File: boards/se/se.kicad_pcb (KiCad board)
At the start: 2 copper layers, 97.2 x 56.5 mm, 35 parts, among them J1 SE_PDS, J2 Conn_02x05_Odd_Even, U1 ENC624J600-PT, U3 GAL16V8, U5 LD1117S33TR_SOT223, Y1 25MHz

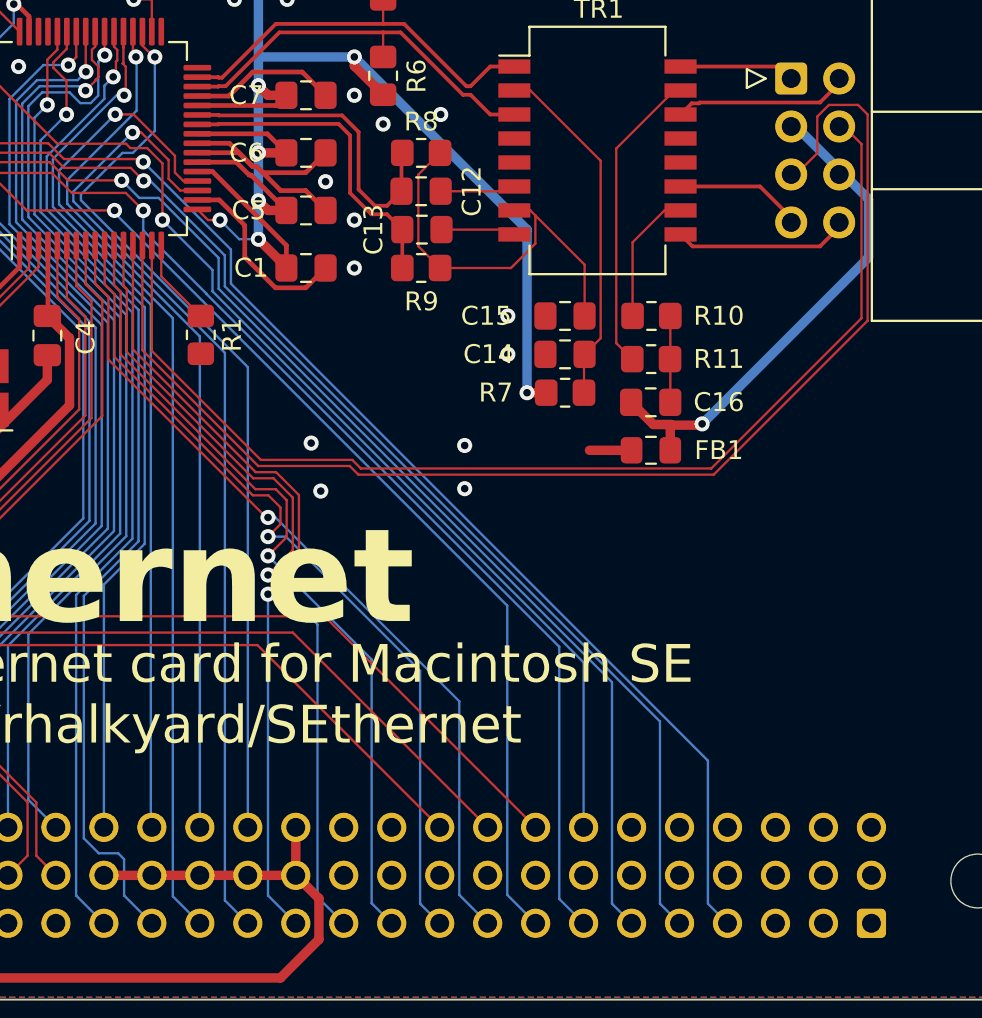
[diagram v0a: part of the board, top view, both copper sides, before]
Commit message: SE: fiddle some track positions for better fills
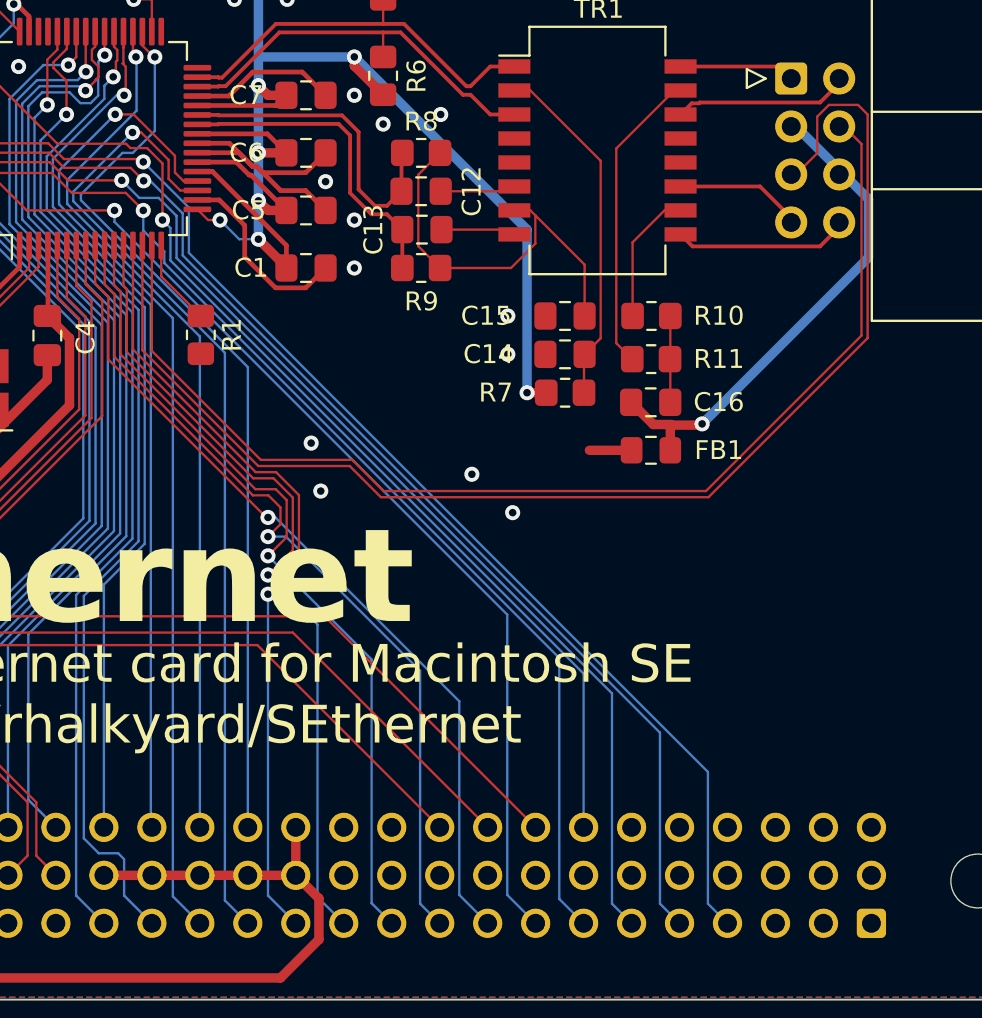
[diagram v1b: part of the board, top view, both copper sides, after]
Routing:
- net /LEDB: track 67.6 -> 69.2 mm
- net /LEDA: track 59.6 -> 61.1 mm

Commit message: Rev1 hardware
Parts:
- added C10: 1uF, Capacitor_SMD:C_0805_2012Metric_Pad1.18x1.45mm_HandSolder, B.Cu at (88.9, 77.7)
- added C11: 1uF, Capacitor_SMD:C_0805_2012Metric_Pad1.18x1.45mm_HandSolder, B.Cu at (77.7, 86.4)
- added C12: 1uF, Capacitor_SMD:C_0805_2012Metric_Pad1.18x1.45mm_HandSolder, B.Cu at (100.1, 89.4)
- added C19: 1uF, Capacitor_SMD:C_0805_2012Metric_Pad1.18x1.45mm_HandSolder, B.Cu at (87.6, 100.1)
- added J3: Conn_01x07, Connector_PinHeader_2.54mm:PinHeader_1x07_P2.54mm_Vertical, F.Cu at (88.9, 113.0)
- added U2: ATF1502AS-xAx44, Package_QFP:TQFP-44_10x10mm_P0.8mm, B.Cu at (88.9, 88.9)
- C1: renamed from C16; footprint Capacitor_SMD:C_0805_2012Metric_Pad1.18x1.45mm_HandSolder -> Capacitor_SMD:C_1206_3216Metric_Pad1.33x1.80mm_HandSolder; moved to B.Cu
- C13: renamed from C4; moved to B.Cu
- C14: renamed from C2; moved to B.Cu
- C15: renamed from C10; moved to B.Cu
- C16: renamed from C8; moved to B.Cu
- C17: renamed from C3; moved to B.Cu
- C18: renamed from C9; moved to B.Cu
- C2: renamed from C15; moved to B.Cu
- C20: renamed from C11; moved to B.Cu
- C21: renamed from C18; moved to B.Cu
- C22: renamed from C17; moved to B.Cu
- C3: renamed from C14; moved to B.Cu
- C4: renamed from C13; moved to B.Cu
- C5: renamed from C12; moved to B.Cu
- C6: renamed from C1; moved to B.Cu
- C7: renamed from C5; moved to B.Cu
- C8: renamed from C6; moved to B.Cu
- C9: renamed from C7; moved to B.Cu
- FB1, J2, R6, TR1, U1, Y1: moved to B.Cu
- J1: value SE_PDS -> Macintosh SE PDS Interface; footprint Connector_DIN:DIN41612_C_3x32_Female_Vertical_THT -> PDS-Ethernet:DIN41612_C_3x32_Female_Vertical_THT_Reversed
- R1: renamed from R10; moved to B.Cu
- R2: renamed from R11; moved to B.Cu
- R3: renamed from R7; moved to B.Cu
- R4: renamed from R9; moved to B.Cu
- R5: renamed from R8; moved to B.Cu
- R7: renamed from R4; moved to B.Cu
- R8: renamed from R1; moved to B.Cu
- R9: renamed from R5; moved to B.Cu
- U3: value GAL16V8 -> 74LVC2G17; footprint Package_LCC:PLCC-20_THT-Socket -> Package_TO_SOT_SMD:SOT-363_SC-70-6; moved to B.Cu
- U4: renamed from U5; moved to B.Cu
- moved C21 88.3 mm to (97.6, 113.0)
- moved C22 86.1 mm to (106.4, 113.0)
- moved U4 82.6 mm to (101.9, 106.8), turned to 180 degrees
- moved U3 77.0 mm to (76.8, 93.4), turned to 180 degrees
- moved C16 71.3 mm to (76.8, 96.5)
- moved C14 70.6 mm to (69.6, 91.7)
- moved C18 67.6 mm to (56.6, 100.8), turned to -90 degrees
- moved C17 65.2 mm to (52.9, 100.8), turned to 90 degrees
- moved R9 64.2 mm to (69.6, 85.1)
- moved U1 60.1 mm to (57.7, 88.9), turned to 0 degrees
- moved C15 56.8 mm to (47.0, 94.0), turned to 0 degrees
- moved Y1 56.8 mm to (47.0, 97.8), turned to 180 degrees
- moved C20 56.8 mm to (47.0, 101.6), turned to 180 degrees
- moved C13 54.9 mm to (47.0, 91.4), turned to 0 degrees
- moved C9 54.1 mm to (59.9, 77.5), turned to 90 degrees
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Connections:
- J1 pad b28: unconnected-(J1-~{EXT_DTK}-Padb28) -> ~{EXT_DTK}
- J1 pad c12: unconnected-(J1-~{RESET}-Padc12) -> ~{RESET}
- J1 pad c6: unconnected-(J1-~{DTACK}-Padc6) -> ~{DTACK}
- R9 pad 1: +3.3V -> GND
- U1 pad 33: unconnected-(U1-CLKOUT-Pad33) -> /ETH_CLK
- U1 pad 48: /B1SEL -> /B1SEL'
- U1 pad 49: Net-(U1-~{CS}/CS) -> /ETH_CS
- U1 pad 50: /B0SEL -> /B0SEL'
- U3 pad 1: A23 -> /B1SEL
- U3 pad 2: A22 -> GND
- U3 pad 3: A21 -> /B0SEL
- U3 pad 4: A20 -> /B0SEL'
- U3 pad 5: A19 -> +5V
- U3 pad 6: A18 -> /B1SEL'
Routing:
- net GND: track 76.8 -> 162.7 mm, vias 37 -> 160
- net ~{EXT_DTK}: track 0.00 -> 52.3 mm, vias 0 -> 1
- net ~{UDS}: track 73.5 -> 24.7 mm, vias 1 -> 0
- net ~{LDS}: track 72.6 -> 25.8 mm, vias 1 -> 0
- net ~{AS}: track 63.8 -> 24.1 mm, vias 1 -> 0
- net /CPLD_VPP: track 0.00 -> 36.6 mm, vias 0 -> 1
- net D12: track 43.7 -> 79.7 mm
- net +5V: track 128.5 -> 164.3 mm, vias 2 -> 0
- net D13: track 46.0 -> 80.6 mm
- net Net-(U1-~{CS}/CS): track 34.5 -> 0.00 mm, vias 1 -> 0
- net /TCK: track 0.00 -> 33.8 mm, vias 0 -> 1
- net D14: track 47.7 -> 81.2 mm
- net D15: track 48.8 -> 81.9 mm
- net /TPOUT-: track 21.1 -> 52.7 mm
- net /TPOUT+: track 21.1 -> 52.6 mm
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- added copper zone on In1.Cu, net GND
- added copper zone on In2.Cu, net GND
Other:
- board size 97.2 x 56.5 mm -> 90 x 99 mm
- copper layers 2 -> 4
- board text added: "+5V"
- board text added: "10/100 Ethernet for Macintosh SE github.com/rhalkyard/SEthernet Revision 1"
- board text added: "3"
- board text added: "Build info:"
- board text added: "CPLD JTAG"
- board text added: "GND"
- board text added: "TCK"
- board text added: "TDI"
- board text added: "TDO"
- board text added: "TMS"
- board text added: "V_{PP}"
- board text removed: "10/100 Ethernet card for Macintosh SE github.com/rhalkyard/SEthernet"
- board text removed: "Revision 0"

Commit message: SPISEL pulldown resistor should be 100K, not 10K
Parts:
- R9: value 10K -> 100K
